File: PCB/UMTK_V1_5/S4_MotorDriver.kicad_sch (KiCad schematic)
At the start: 17 parts, among them J1 Motor Out, J2 Motor Shunt, U1 DRV8873SPWPRQ1

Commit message: Initial Place, Board Stack
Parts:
- C10, C12, C8, C9: footprint Diode_SMD:D_1206_3216Metric -> Capacitor_SMD:C_0603_1608Metric
- J2: value Motor Shunt -> ESTOP
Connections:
- net GND: now also U1.25 (EP), U1.25.1 (EP), U1.25.10 (EP), U1.25.11 (EP), U1.25.12 (EP), U1.25.13 (EP), U1.25.14 (EP), U1.25.15 (EP), U1.25.16 (EP), U1.25.17 (EP), U1.25.18 (EP), U1.25.2 (EP), U1.25.3 (EP), U1.25.4 (EP), U1.25.5 (EP), U1.25.6 (EP), U1.25.7 (EP), U1.25.8 (EP), U1.25.9 (EP)
- net VM+: now also J1.1 (Pin_1); no longer J1.2 (Pin_2)
- net VM-: now also J1.2 (Pin_2); no longer J1.1 (Pin_1)
- no-connect marks 1 -> 0
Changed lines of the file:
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@@
 		(color 0 0 0 0)
 	)
-	(no_connect
-		(at 173.99 161.29)
+	(junction
+		(at 182.88 163.83)
+		(diameter 0)
+		(color 0 0 0 0)
 	)
 	(wire
@@
 	(wire
 		(pts
+			(xy 173.99 161.29) (xy 182.88 161.29)
+		)
+		(stroke
+			(width 0)
+			(type default)
+		)
+	)
+	(wire
+		(pts
 			(xy 93.98 119.38) (xy 93.98 123.19)
 		)
@@
 		(pts
 			(xy 81.28 146.05) (xy 81.28 154.94)
+		)
+		(stroke
+			(width 0)
+			(type default)
+		)
+	)
+	(wire
+		(pts
+			(xy 182.88 161.29) (xy 182.88 163.83)
 		)
 		(stroke
@@
 				(path "/2bf3ea67-58b8-47b3-a768-ea6950b40edf/429db1c7-ec58-4147-903c-f97ceea1f1c2"
 					(reference "R21")
+					(unit 1)
+				)
+			)
+		)
+	)
+	(symbol
+		(lib_id "Connector:Screw_Terminal_01x02")
+		(at 234.95 52.07 0)
+		(mirror y)
+		(unit 1)
+		(exclude_from_sim no)
+		(in_bom yes)
+		(on_board yes)
+		(dnp no)
+		(property "Reference" "J1"
+			(at 234.95 49.53 0)
+			(effects
+				(font
+					(size 1.27 1.27)
+				)
+			)
+		)
+		(property "Value" "Motor Out"
+			(at 234.95 57.15 0)
+			(effects
+				(font
+					(size 1.27 1.27)
+				)
+			)
+		)
+		(property "Footprint" "TerminalBlock_Altech:Altech_AK100_1x02_P5.00mm"
+			(at 234.95 52.07 0)
+			(effects
+				(font
+					(size 1.27 1.27)
+				)
+				(hide yes)
+			)
+		)
+		(property "Datasheet" "~"
+			(at 234.95 52.07 0)
+			(effects
+				(font
+					(size 1.27 1.27)
+				)
+				(hide yes)
+			)
+		)
+		(property "Description" "Generic screw terminal, single row, 01x02, script generated (kicad-library-utils/schlib/autogen/connector/)"
+			(at 234.95 52.07 0)
+			(effects
+				(font
+					(size 1.27 1.27)
+				)
+				(hide yes)
+			)
+		)
+		(pin "1"
+		)
+		(pin "2"
+		)
+		(instances
+			(project "UMTK"
+				(path "/2bf3ea67-58b8-47b3-a768-ea6950b40edf/429db1c7-ec58-4147-903c-f97ceea1f1c2"
+					(reference "J1")
 					(unit 1)
 				)
@@
 			)
 		)
-		(property "Footprint" "Diode_SMD:D_1206_3216Metric"
+		(property "Footprint" "Capacitor_SMD:C_0603_1608Metric"
 			(at 232.1052 125.73 0)
 			(effects
@@
 				(path "/2bf3ea67-58b8-47b3-a768-ea6950b40edf/429db1c7-ec58-4147-903c-f97ceea1f1c2"
 					(reference "#PWR023")
-					(unit 1)
-				)
-			)
-		)
-	)
-	(symbol
-		(lib_id "Connector:Screw_Terminal_01x02")
-		(at 234.95 54.61 180)
-		(unit 1)
-		(exclude_from_sim no)
-		(in_bom yes)
-		(on_board yes)
-		(dnp no)
-		(property "Reference" "J1"
-			(at 234.95 57.15 0)
-			(effects
-				(font
-					(size 1.27 1.27)
-				)
-			)
-		)
-		(property "Value" "Motor Out"
-			(at 234.95 49.53 0)
-			(effects
-				(font
-					(size 1.27 1.27)
-				)
-			)
-		)
-		(property "Footprint" "TerminalBlock_Altech:Altech_AK100_1x02_P5.00mm"
-			(at 234.95 54.61 0)
-			(effects
-				(font
-					(size 1.27 1.27)
-				)
-				(hide yes)
-			)
-		)
-		(property "Datasheet" "~"
-			(at 234.95 54.61 0)
-			(effects
-				(font
-					(size 1.27 1.27)
-				)
-				(hide yes)
-			)
-		)
-		(property "Description" "Generic screw terminal, single row, 01x02, script generated (kicad-library-utils/schlib/autogen/connector/)"
-			(at 234.95 54.61 0)
-			(effects
-				(font
-					(size 1.27 1.27)
-				)
-				(hide yes)
-			)
-		)
-		(pin "1"
-		)
-		(pin "2"
-		)
-		(instances
-			(project "UMTK"
-				(path "/2bf3ea67-58b8-47b3-a768-ea6950b40edf/429db1c7-ec58-4147-903c-f97ceea1f1c2"
-					(reference "J1")
 					(unit 1)
 				)
@@
 			)
 		)
-		(property "Footprint" "Diode_SMD:D_1206_3216Metric"
+		(property "Footprint" "Capacitor_SMD:C_0603_1608Metric"
 			(at 200.9648 123.19 0)
 			(effects
@@
 			)
 		)
-		(property "Footprint" "Diode_SMD:D_1206_3216Metric"
+		(property "Footprint" "Capacitor_SMD:C_0603_1608Metric"
 			(at 186.69 122.2248 0)
 			(effects
@@
 			)
 		)
-		(property "Footprint" "Diode_SMD:D_1206_3216Metric"
+		(property "Footprint" "Capacitor_SMD:C_0603_1608Metric"
 			(at 207.3148 123.19 0)
 			(effects
@@
 			)
 		)
-		(property "Value" "Motor Shunt"
+		(property "Value" "ESTOP"
 			(at 250.19 74.93 0)
 			(effects

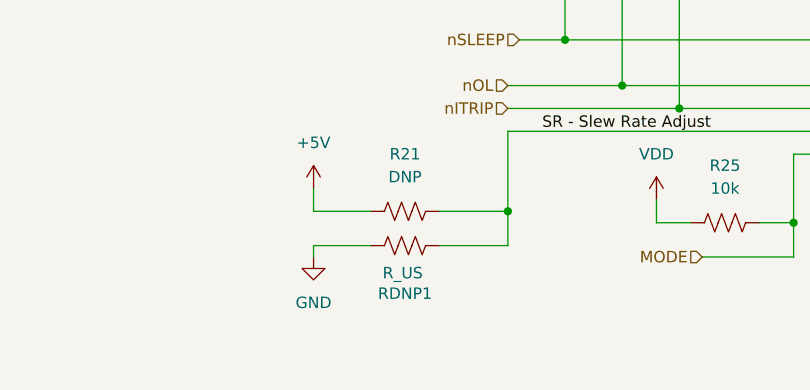
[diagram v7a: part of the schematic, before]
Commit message: Placement Approved, Added holes
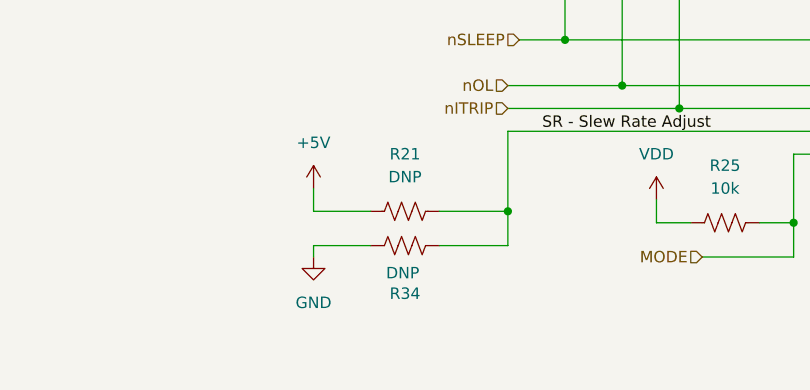
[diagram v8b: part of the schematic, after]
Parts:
- R34: renamed from RDNP1; value R_US -> DNP
- U1: footprint Package_SO:HTSSOP-24-1EP_4.4x7.8mm_P0.65mm_EP3.4x7.8mm_Mask2.4x2.98mm_ThermalVias -> Package_SO:HTSSOP-24-1EP_4.4x7.8mm_P0.65mm_EP3.4x7.8mm_Mask2.4x4.68mm_ThermalVias
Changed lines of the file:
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@@
 			)
 		)
-		(property "Footprint" "Package_SO:HTSSOP-24-1EP_4.4x7.8mm_P0.65mm_EP3.4x7.8mm_Mask2.4x2.98mm_ThermalVias"
+		(property "Footprint" "Package_SO:HTSSOP-24-1EP_4.4x7.8mm_P0.65mm_EP3.4x7.8mm_Mask2.4x4.68mm_ThermalVias"
 			(at 156.21 140.97 0)
 			(effects
@@
 		(on_board yes)
 		(dnp no)
-		(property "Reference" "RDNP1"
+		(property "Reference" "R34"
 			(at 69.85 164.084 90)
 			(effects
@@
 			)
 		)
-		(property "Value" "R_US"
+		(property "Value" "DNP"
 			(at 69.596 161.798 90)
 			(effects
@@
 			(project "UMTK"
 				(path "/2bf3ea67-58b8-47b3-a768-ea6950b40edf/429db1c7-ec58-4147-903c-f97ceea1f1c2"
-					(reference "RDNP1")
-					(unit 1)
-				)
+					(reference "R34")
+					(unit 1)
+				)
